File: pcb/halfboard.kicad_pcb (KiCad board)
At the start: 2 copper layers, 117.4 x 87.9 mm, 54 parts, among them U1 

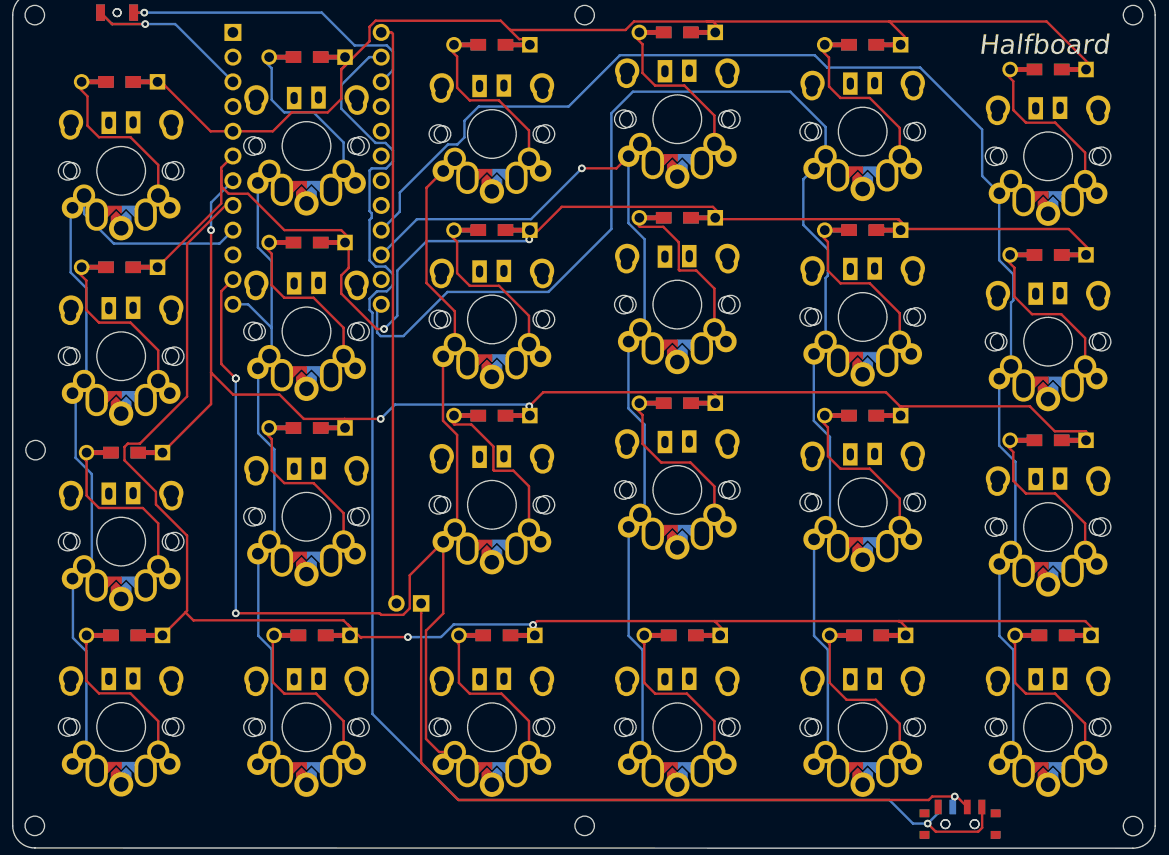
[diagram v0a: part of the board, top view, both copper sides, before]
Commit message: update footprint for better fit
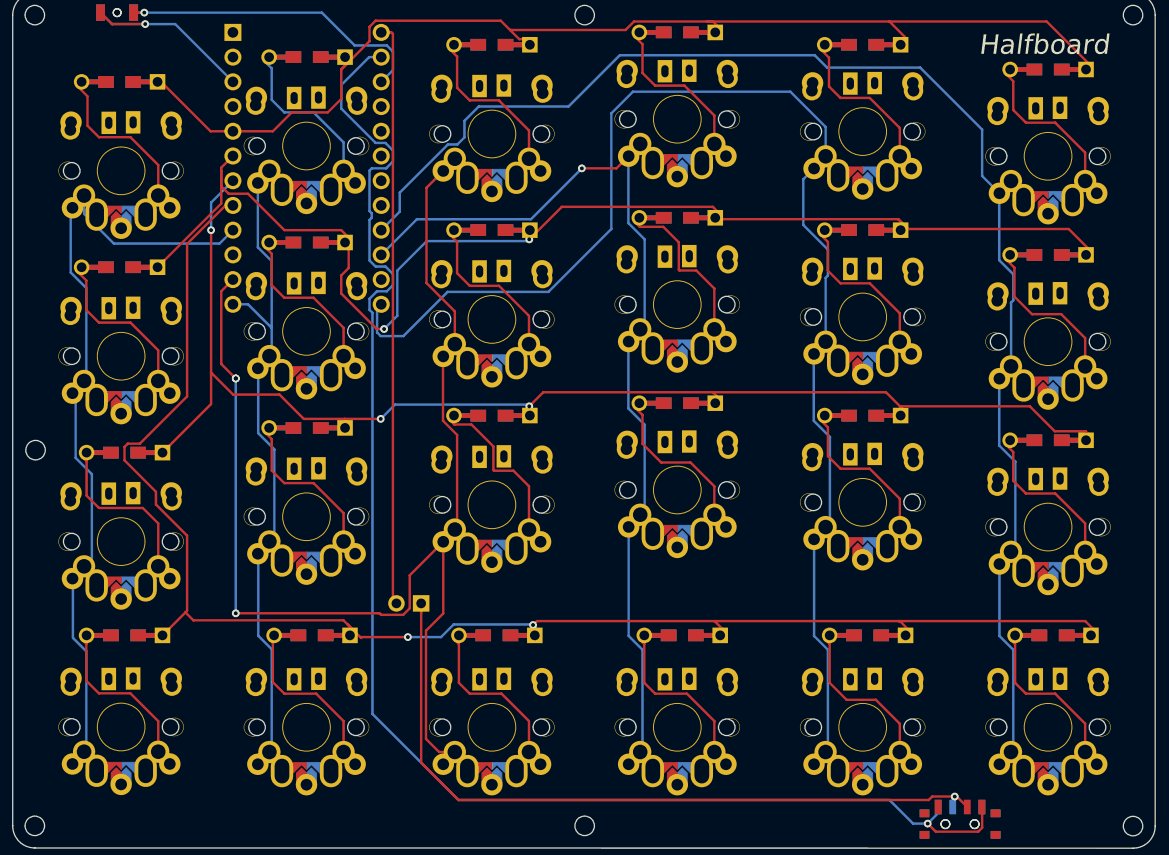
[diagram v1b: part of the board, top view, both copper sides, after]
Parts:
- removed the   at (135.4, 130.6) (x2)
- added  : , Button_Switch_SMD:SW_SPDT_PCM12, F.Cu at (135.4, 130.6)
- added  : , Button_Switch_SMD:SW_SPDT_PCM12, B.Cu at (135.4, 130.6)

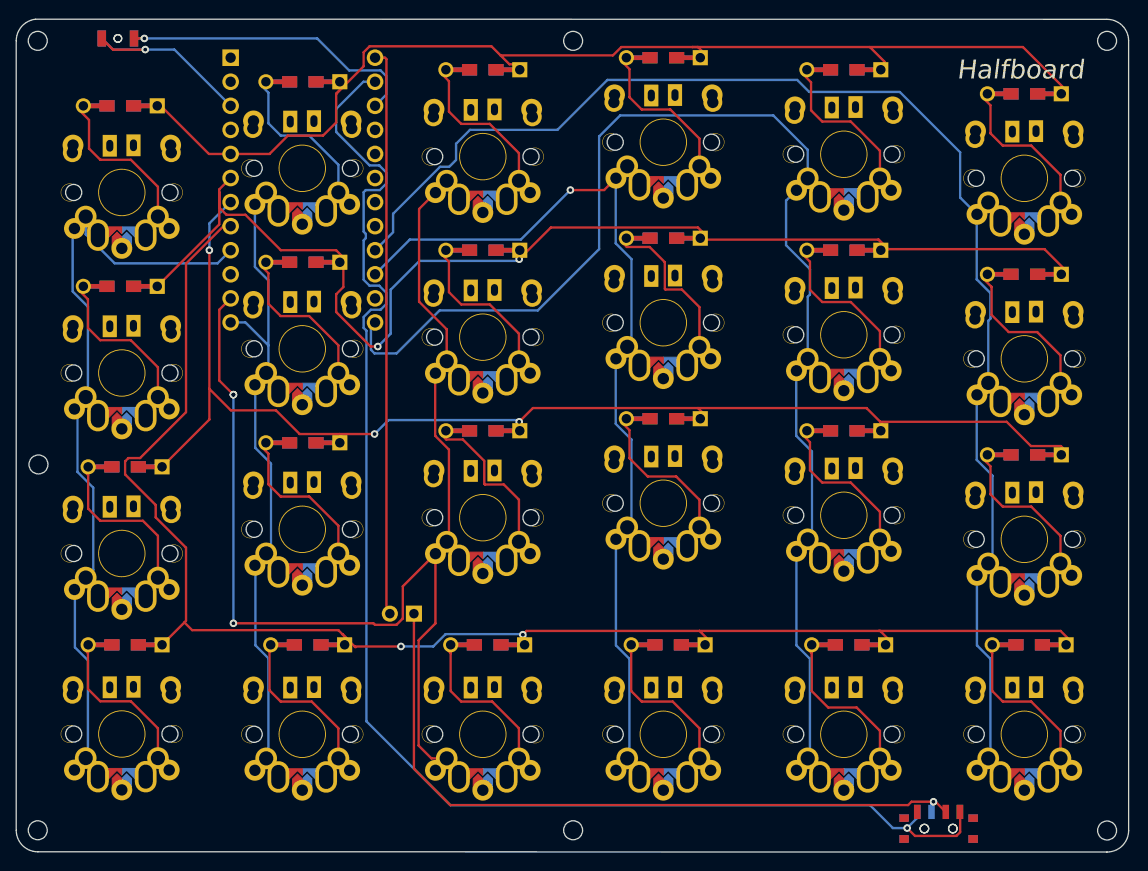
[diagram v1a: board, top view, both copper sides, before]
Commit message: redo routing using freerouting
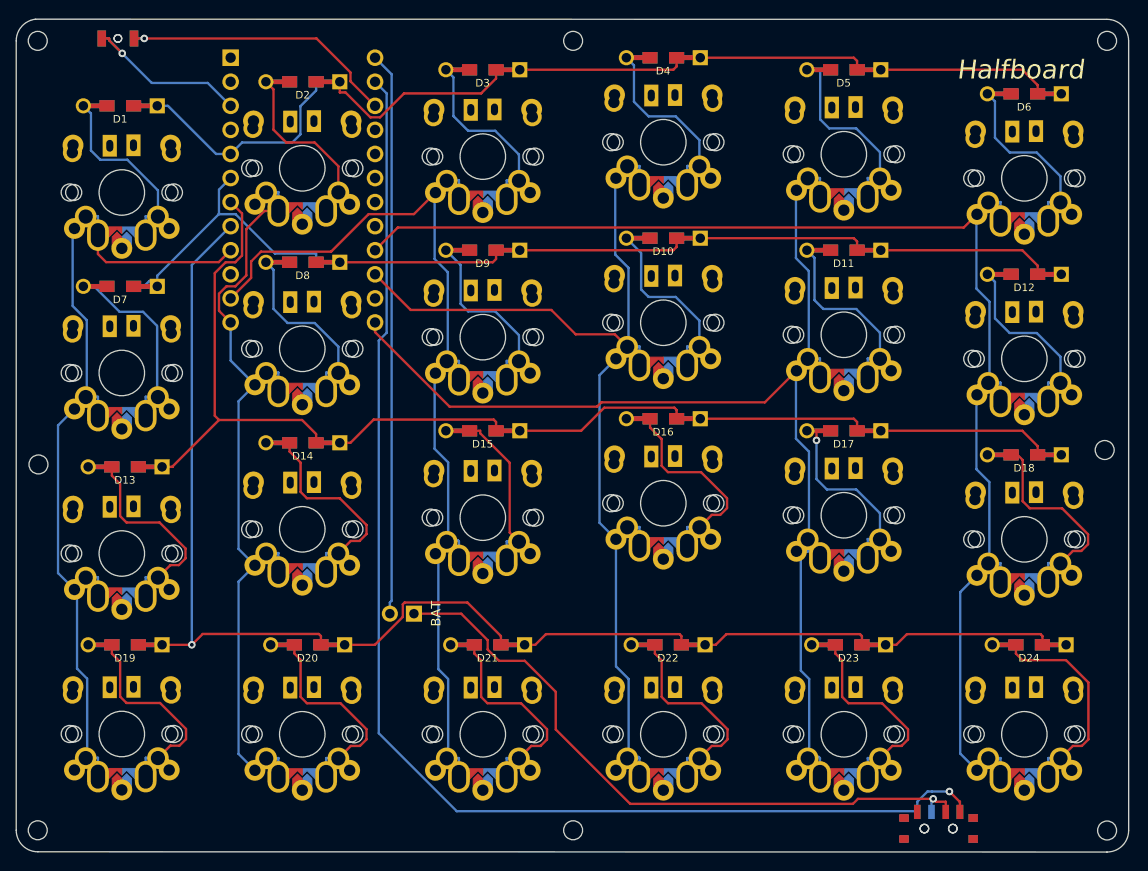
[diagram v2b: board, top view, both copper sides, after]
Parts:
- removed  : , halfboard:MX-ALPs-PG1350-LED-FLIP (x22)
- removed  : , Button_Switch_SMD:SW_SPDT_PCM12 (x2)
- removed  : D, halfboard:Diode-dual (x19)
- removed  : , halfboard:Diode-dual (x3)
- added  D11: , halfboard:Diode-dual, F.Cu at (125.4, 69.8)
- added  D12: , halfboard:Diode-dual, F.Cu at (144.4, 72.4)
- added B.PWR SW: , Button_Switch_SMD:SW_SPDT_PCM12, B.Cu at (135.4, 130.6)
- added D10: , halfboard:Diode-dual, F.Cu at (106.3, 68.6)
- added D13: , halfboard:Diode-dual, F.Cu at (49.5, 92.7)
- added D14: , halfboard:Diode-dual, F.Cu at (68.3, 90.2)
- added D15: , halfboard:Diode-dual, F.Cu at (87.3, 88.9)
- added D16: , halfboard:Diode-dual, F.Cu at (106.3, 87.6)
- added D17: , halfboard:Diode-dual, F.Cu at (125.4, 88.9)
- added D18: , halfboard:Diode-dual, F.Cu at (144.4, 91.4)
- added D19: , halfboard:Diode-dual, F.Cu at (49.5, 111.5)
- added D2: , halfboard:Diode-dual, F.Cu at (68.3, 52.1)
- added D20: , halfboard:Diode-dual, F.Cu at (68.8, 111.5)
- added D21: , halfboard:Diode-dual, F.Cu at (87.8, 111.5)
- added D22: , halfboard:Diode-dual, F.Cu at (106.8, 111.5)
- added D23: , halfboard:Diode-dual, F.Cu at (125.9, 111.5)
- added D24: , halfboard:Diode-dual, F.Cu at (144.9, 111.5)
- added D3: , halfboard:Diode-dual, F.Cu at (87.3, 50.8)
- added D4: , halfboard:Diode-dual, F.Cu at (106.3, 49.5)
- added D5: , halfboard:Diode-dual, F.Cu at (125.4, 50.8)
- added D6: , halfboard:Diode-dual, F.Cu at (144.4, 53.3)
- added D8: , halfboard:Diode-dual, F.Cu at (68.3, 71.1)
- added D9: , halfboard:Diode-dual, F.Cu at (87.3, 69.8)
- added F.PWR SW: , Button_Switch_SMD:SW_SPDT_PCM12, F.Cu at (135.4, 130.6)
- added SW1: , halfboard:MX-ALPs-PG1350-LED-FLIP, F.Cu at (68.2, 61.2)
- added SW10: , halfboard:MX-ALPs-PG1350-LED-FLIP, F.Cu at (125.4, 78.8)
- added SW11: , halfboard:MX-ALPs-PG1350-LED-FLIP, F.Cu at (144.4, 81.3)
- added SW12: , halfboard:MX-ALPs-PG1350-LED-FLIP, F.Cu at (49.2, 101.9)
- added SW13: , halfboard:MX-ALPs-PG1350-LED-FLIP, F.Cu at (68.2, 99.3)
- added SW14: , halfboard:MX-ALPs-PG1350-LED-FLIP, F.Cu at (87.3, 98.1)
- added SW15: , halfboard:MX-ALPs-PG1350-LED-FLIP, F.Cu at (106.3, 96.5)
- added SW16: , halfboard:MX-ALPs-PG1350-LED-FLIP, F.Cu at (125.4, 97.8)
- added SW17: , halfboard:MX-ALPs-PG1350-LED-FLIP, F.Cu at (144.4, 100.4)
- added SW18: , halfboard:MX-ALPs-PG1350-LED-FLIP, F.Cu at (49.2, 120.9)
- added SW19: , halfboard:MX-ALPs-PG1350-LED-FLIP, F.Cu at (68.2, 120.9)
- added SW2: , halfboard:MX-ALPs-PG1350-LED-FLIP, F.Cu at (87.3, 60.0)
- added SW20: , halfboard:MX-ALPs-PG1350-LED-FLIP, F.Cu at (87.3, 120.9)
- added SW21: , halfboard:MX-ALPs-PG1350-LED-FLIP, F.Cu at (106.3, 120.9)
- added SW22: , halfboard:MX-ALPs-PG1350-LED-FLIP, F.Cu at (125.4, 120.9)
- added SW23: , halfboard:MX-ALPs-PG1350-LED-FLIP, F.Cu at (144.4, 120.9)
- added SW3: , halfboard:MX-ALPs-PG1350-LED-FLIP, F.Cu at (106.3, 58.4)
- added SW4: , halfboard:MX-ALPs-PG1350-LED-FLIP, F.Cu at (125.4, 59.7)
- added SW5: , halfboard:MX-ALPs-PG1350-LED-FLIP, F.Cu at (144.4, 62.3)
- added SW7: , halfboard:MX-ALPs-PG1350-LED-FLIP, F.Cu at (68.2, 80.3)
- added SW8: , halfboard:MX-ALPs-PG1350-LED-FLIP, F.Cu at (87.3, 79.0)
- added SW9: , halfboard:MX-ALPs-PG1350-LED-FLIP, F.Cu at (106.3, 77.5)
- B.RST, BAT, D1, D7, F.RST, SW0, SW6: renamed from  
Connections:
- D1 pad 1: (no net) -> row0
- D1 pad 2: (no net) -> col0_row0
- D7 pad 1: (no net) -> row1
- D7 pad 2: (no net) -> col0_row1
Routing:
- net col3: track 90.8 -> 112.5 mm, vias 1 -> 0
- net col1: track 66.7 -> 87.7 mm
- net col2: track 126.4 -> 106.9 mm, vias 3 -> 0
- net col0: track 80.0 -> 94.6 mm
- net BAT_GND: track 150.2 -> 137.4 mm
- net row0: track 117.9 -> 129.0 mm
- net col5_row3: track 16.9 -> 27.2 mm
- net col4_row1: track 16.6 -> 26.7 mm
- net col0_row1: track 17.0 -> 27.1 mm
- net col5_row2: track 16.6 -> 26.5 mm
- net col1_row1: track 16.8 -> 26.6 mm
- net col5_row0: track 16.6 -> 26.4 mm
- net col2_row0: track 16.8 -> 26.6 mm
- net col2_row1: track 16.8 -> 26.6 mm
- net col3_row0: track 16.6 -> 26.4 mm
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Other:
- outline, holes or cut-outs redrawn

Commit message: create schematics and assign footprints in pcb
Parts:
- removed the D1 at (49.0, 54.6)
- removed the D10 at (106.3, 68.6)
- removed the D13 at (49.5, 92.7)
- removed the D14 at (68.3, 90.2)
- removed the D15 at (87.3, 88.9)
- removed the D16 at (106.3, 87.6)
- removed the D17 at (125.4, 88.9)
- removed the D18 at (144.4, 91.4)
- removed the D19 at (49.5, 111.5)
- removed the D2 at (68.3, 52.1)
- removed the D20 at (68.8, 111.5)
- removed the D21 at (87.8, 111.5)
- removed the D22 at (106.8, 111.5)
- removed the D23 at (125.9, 111.5)
- removed the D24 at (144.9, 111.5)
- removed the D3 at (87.3, 50.8)
- removed the D4 at (106.3, 49.5)
- removed the D5 at (125.4, 50.8)
- removed the D6 at (144.4, 53.3)
- removed the D7 at (49.0, 73.7)
- removed the D8 at (68.3, 71.1)
- removed the D9 at (87.3, 69.8)
- removed SW0: , halfboard:MX-ALPs-PG1350-LED-FLIP
- removed the SW1 at (68.2, 61.2)
- removed the SW10 at (125.4, 78.8)
- removed the SW11 at (144.4, 81.3)
- removed the SW12 at (49.2, 101.9)
- removed the SW13 at (68.2, 99.3)
- removed the SW14 at (87.3, 98.1)
- removed the SW15 at (106.3, 96.5)
- removed the SW16 at (125.4, 97.8)
- removed the SW17 at (144.4, 100.4)
- removed the SW18 at (49.2, 120.9)
- removed the SW19 at (68.2, 120.9)
- removed the SW2 at (87.3, 60.0)
- removed the SW20 at (87.3, 120.9)
- removed the SW21 at (106.3, 120.9)
- removed the SW22 at (125.4, 120.9)
- removed the SW23 at (144.4, 120.9)
- removed the SW3 at (106.3, 58.4)
- removed the SW4 at (125.4, 59.7)
- removed the SW5 at (144.4, 62.3)
- removed the SW6 at (49.2, 82.8)
- removed the SW7 at (68.2, 80.3)
- removed the SW8 at (87.3, 79.0)
- removed the SW9 at (106.3, 77.5)
- removed the U1 at (68.3, 63.5)
- added  : , halfboard:MX-ALPs-PG1350-LED-FLIP-PLATE, F.Cu at (205.6, 106.4)
- added  : , halfboard:MX-ALPs-PG1350-LED-FLIP-PLATE, F.Cu at (262.8, 120.1)
- added  : , halfboard:MX-ALPs-PG1350-LED-FLIP-PLATE, F.Cu at (224.7, 122.9)
- added  : , halfboard:MX-ALPs-PG1350-LED-FLIP-PLATE, F.Cu at (281.8, 102.4)
- added  : , halfboard:MX-ALPs-PG1350-LED-FLIP-PLATE, F.Cu at (300.9, 124.0)
- added  : , halfboard:MX-ALPs-PG1350-LED-FLIP-PLATE, F.Cu at (300.9, 144.5)
- added  : , halfboard:MX-ALPs-PG1350-LED-FLIP-PLATE, F.Cu at (224.7, 144.5)
- added  : , halfboard:MX-ALPs-PG1350-LED-FLIP-PLATE, F.Cu at (262.8, 82.0)
- added  : , halfboard:MX-ALPs-PG1350-LED-FLIP-PLATE, F.Cu at (243.7, 83.6)
- added  : , halfboard:MX-ALPs-PG1350-LED-FLIP-PLATE, F.Cu at (281.8, 121.4)
- added  : , halfboard:MX-ALPs-PG1350-LED-FLIP-PLATE, F.Cu at (205.6, 125.5)
- added  : , halfboard:MX-ALPs-PG1350-LED-FLIP-PLATE, F.Cu at (262.8, 101.1)
- added  : , halfboard:MX-ALPs-PG1350-LED-FLIP-PLATE, F.Cu at (205.6, 144.5)
- added  : , halfboard:MX-ALPs-PG1350-LED-FLIP-PLATE, F.Cu at (224.7, 103.8)
- added  : , halfboard:MX-ALPs-PG1350-LED-FLIP-PLATE, F.Cu at (224.7, 84.8)
- added  : , halfboard:MX-ALPs-PG1350-LED-FLIP-PLATE, F.Cu at (281.8, 144.5)
- added  : , halfboard:MX-ALPs-PG1350-LED-FLIP-PLATE, F.Cu at (300.9, 104.9)
- added  : , halfboard:MX-ALPs-PG1350-LED-FLIP-PLATE, F.Cu at (243.7, 102.6)
- added  : , halfboard:MX-ALPs-PG1350-LED-FLIP-PLATE, F.Cu at (262.8, 144.5)
- added  : , halfboard:MX-ALPs-PG1350-LED-FLIP-PLATE, F.Cu at (300.9, 85.9)
- added  : , halfboard:MX-ALPs-PG1350-LED-FLIP-PLATE, F.Cu at (243.7, 121.7)
- added  : , halfboard:MX-ALPs-PG1350-LED-FLIP-PLATE, F.Cu at (205.6, 87.4)
- added  : , halfboard:MX-ALPs-PG1350-LED-FLIP-PLATE, F.Cu at (281.8, 83.3)
- added  : , halfboard:MX-ALPs-PG1350-LED-FLIP-PLATE, F.Cu at (243.7, 144.5)
- added BAT1: Battery, Connector_PinHeader_2.54mm:PinHeader_1x02_P2.54mm_Vertical, F.Cu at (234.9, 131.7)
- added D1: 1N4148W, halfboard:Diode-dual, F.Cu at (184.3, 96.9)
- added D1: , halfboard:Diode-dual, F.Cu at (27.5, 116.9)
- added D10: 1N4148W, halfboard:Diode-dual, F.Cu at (176.1, 94.3)
- added D10: , halfboard:Diode-dual, F.Cu at (84.8, 130.9)
- added D11: 1N4148W, halfboard:Diode-dual, F.Cu at (173.3, 77.3)
- added D12: 1N4148W, halfboard:Diode-dual, F.Cu at (121.9, 97.8)
- added D13: 1N4148W, halfboard:Diode-dual, F.Cu at (163.5, 102.1)
- added D13: , halfboard:Diode-dual, F.Cu at (28.0, 155.0)
- added D14: 1N4148W, halfboard:Diode-dual, F.Cu at (132.3, 97.8)
- added D14: , halfboard:Diode-dual, F.Cu at (46.8, 152.5)
- added D15: 1N4148W, halfboard:Diode-dual, F.Cu at (132.3, 100.4)
- added D15: , halfboard:Diode-dual, F.Cu at (65.8, 151.2)
- added D16: 1N4148W, halfboard:Diode-dual, F.Cu at (155.3, 94.3)
- added D16: , halfboard:Diode-dual, F.Cu at (84.8, 149.9)
- added D17: 1N4148W, halfboard:Diode-dual, F.Cu at (142.7, 97.8)
- added D17: , halfboard:Diode-dual, F.Cu at (103.9, 151.2)
- added D18: 1N4148W, halfboard:Diode-dual, F.Cu at (153.1, 97.8)
- added D18: , halfboard:Diode-dual, F.Cu at (122.9, 153.7)
- added D19: 1N4148W, halfboard:Diode-dual, F.Cu at (142.7, 100.4)
- added D19: , halfboard:Diode-dual, F.Cu at (28.0, 173.8)
- added D2: 1N4148W, halfboard:Diode-dual, F.Cu at (173.3, 87.7)
- added D2: , halfboard:Diode-dual, F.Cu at (46.8, 114.4)
- added D20: 1N4148W, halfboard:Diode-dual, F.Cu at (165.7, 94.3)
- added D20: , halfboard:Diode-dual, F.Cu at (47.3, 173.8)
- added D21: 1N4148W, halfboard:Diode-dual, F.Cu at (153.1, 100.4)
- added D21: , halfboard:Diode-dual, F.Cu at (66.3, 173.8)
- added D22: 1N4148W, halfboard:Diode-dual, F.Cu at (163.5, 96.9)
- added D22: , halfboard:Diode-dual, F.Cu at (85.3, 173.8)
- added D23: 1N4148W, halfboard:Diode-dual, F.Cu at (163.5, 99.5)
- added D23: , halfboard:Diode-dual, F.Cu at (104.4, 173.8)
- added D24: 1N4148W, halfboard:Diode-dual, F.Cu at (121.9, 100.4)
- added D24: , halfboard:Diode-dual, F.Cu at (123.4, 173.8)
- added D3: 1N4148W, halfboard:Diode-dual, F.Cu at (173.3, 85.1)
- added D3: , halfboard:Diode-dual, F.Cu at (65.8, 113.1)
- added D4: 1N4148W, halfboard:Diode-dual, F.Cu at (173.3, 82.5)
- added D4: , halfboard:Diode-dual, F.Cu at (84.8, 111.8)
- added D5: 1N4148W, halfboard:Diode-dual, F.Cu at (173.3, 79.9)
- added D5: , halfboard:Diode-dual, F.Cu at (103.9, 113.1)
- added D6: 1N4148W, halfboard:Diode-dual, F.Cu at (173.9, 102.1)
- added D6: , halfboard:Diode-dual, F.Cu at (122.9, 115.6)
- added D7: 1N4148W, halfboard:Diode-dual, F.Cu at (173.9, 99.5)
- added D7: , halfboard:Diode-dual, F.Cu at (27.5, 136.0)
- added D8: 1N4148W, halfboard:Diode-dual, F.Cu at (173.9, 96.9)
- added D8: , halfboard:Diode-dual, F.Cu at (46.8, 133.4)
- added D9: 1N4148W, halfboard:Diode-dual, F.Cu at (186.5, 94.3)
- added D9: , halfboard:Diode-dual, F.Cu at (65.8, 132.2)
- added PWR_SW1: SW_SPST, Button_Switch_SMD:SW_SPDT_PCM12, F.Cu at (291.6, 154.2)
- added PWR_SW2: SW_SPST, Button_Switch_SMD:SW_SPDT_PCM12, B.Cu at (291.6, 154.3)
- added RESET1: SW_PUSH, Button_Switch_SMD:SW_SPST_TL3342, F.Cu at (205.9, 74.6)
- added RESET2: SW_PUSH, Button_Switch_SMD:SW_SPST_TL3342, B.Cu at (205.9, 74.6)
- added SW1: SW_PUSH, halfboard:MX-ALPs-PG1350-LED-FLIP, F.Cu at (205.6, 87.4)
- added SW1: , halfboard:MX-ALPs-PG1350-LED-FLIP, F.Cu at (27.7, 126.1)
- added SW10: SW_PUSH, halfboard:MX-ALPs-PG1350-LED-FLIP, F.Cu at (263.1, 99.0)
- added SW10: , halfboard:MX-ALPs-PG1350-LED-FLIP, F.Cu at (84.8, 139.8)
- added SW11: SW_PUSH, halfboard:MX-ALPs-PG1350-LED-FLIP, F.Cu at (283.0, 99.7)
- added SW11: , halfboard:MX-ALPs-PG1350-LED-FLIP, F.Cu at (103.9, 141.1)
- added SW12: SW_PUSH, halfboard:MX-ALPs-PG1350-LED-FLIP, F.Cu at (302.4, 101.4)
- added SW12: , halfboard:MX-ALPs-PG1350-LED-FLIP, F.Cu at (122.9, 143.6)
- added SW13: SW_PUSH, halfboard:MX-ALPs-PG1350-LED-FLIP, F.Cu at (205.6, 125.5)
- added SW13: , halfboard:MX-ALPs-PG1350-LED-FLIP, F.Cu at (27.7, 164.2)
- added SW14: SW_PUSH, halfboard:MX-ALPs-PG1350-LED-FLIP, F.Cu at (224.6, 122.9)
- added SW14: , halfboard:MX-ALPs-PG1350-LED-FLIP, F.Cu at (46.7, 161.6)
- added SW15: SW_PUSH, halfboard:MX-ALPs-PG1350-LED-FLIP, F.Cu at (245.0, 117.7)
- added SW15: , halfboard:MX-ALPs-PG1350-LED-FLIP, F.Cu at (65.8, 160.4)
- added SW16: SW_PUSH, halfboard:MX-ALPs-PG1350-LED-FLIP, F.Cu at (263.2, 116.7)
- added SW16: , halfboard:MX-ALPs-PG1350-LED-FLIP, F.Cu at (84.8, 158.9)
- added SW17: SW_PUSH, halfboard:MX-ALPs-PG1350-LED-FLIP, F.Cu at (283.3, 117.7)
- added SW17: , halfboard:MX-ALPs-PG1350-LED-FLIP, F.Cu at (103.9, 160.1)
- added SW18: SW_PUSH, halfboard:MX-ALPs-PG1350-LED-FLIP, F.Cu at (302.8, 120.7)
- added SW18: , halfboard:MX-ALPs-PG1350-LED-FLIP, F.Cu at (122.9, 162.7)
- added SW19: SW_PUSH, halfboard:MX-ALPs-PG1350-LED-FLIP, F.Cu at (205.6, 144.5)
- added SW19: , halfboard:MX-ALPs-PG1350-LED-FLIP, F.Cu at (27.7, 183.2)
- added SW2: SW_PUSH, halfboard:MX-ALPs-PG1350-LED-FLIP, F.Cu at (224.8, 84.9)
- added SW2: , halfboard:MX-ALPs-PG1350-LED-FLIP, F.Cu at (46.7, 123.5)
- added SW20: SW_PUSH, halfboard:MX-ALPs-PG1350-LED-FLIP, F.Cu at (224.7, 144.5)
- added SW20: , halfboard:MX-ALPs-PG1350-LED-FLIP, F.Cu at (46.7, 183.2)
- added SW21: SW_PUSH, halfboard:MX-ALPs-PG1350-LED-FLIP, F.Cu at (244.3, 145.0)
- added SW21: , halfboard:MX-ALPs-PG1350-LED-FLIP, F.Cu at (65.8, 183.2)
- added SW22: SW_PUSH, halfboard:MX-ALPs-PG1350-LED-FLIP, F.Cu at (262.4, 133.3)
- added SW22: , halfboard:MX-ALPs-PG1350-LED-FLIP, F.Cu at (84.8, 183.2)
- added SW23: SW_PUSH, halfboard:MX-ALPs-PG1350-LED-FLIP, F.Cu at (283.0, 135.0)
- added SW23: , halfboard:MX-ALPs-PG1350-LED-FLIP, F.Cu at (103.9, 183.2)
- added SW24: SW_PUSH, halfboard:MX-ALPs-PG1350-LED-FLIP, F.Cu at (303.0, 137.0)
- added SW24: , halfboard:MX-ALPs-PG1350-LED-FLIP, F.Cu at (122.9, 183.2)
- added SW3: SW_PUSH, halfboard:MX-ALPs-PG1350-LED-FLIP, F.Cu at (244.0, 83.7)
- added SW3: , halfboard:MX-ALPs-PG1350-LED-FLIP, F.Cu at (65.8, 122.3)
- added SW4: SW_PUSH, halfboard:MX-ALPs-PG1350-LED-FLIP, F.Cu at (261.6, 82.5)
- added SW4: , halfboard:MX-ALPs-PG1350-LED-FLIP, F.Cu at (84.8, 120.8)
- added SW5: SW_PUSH, halfboard:MX-ALPs-PG1350-LED-FLIP, F.Cu at (281.8, 84.0)
- added SW5: , halfboard:MX-ALPs-PG1350-LED-FLIP, F.Cu at (103.9, 122.0)
- added SW6: SW_PUSH, halfboard:MX-ALPs-PG1350-LED-FLIP, F.Cu at (300.5, 85.6)
- added SW6: , halfboard:MX-ALPs-PG1350-LED-FLIP, F.Cu at (122.9, 124.6)
- added SW7: SW_PUSH, halfboard:MX-ALPs-PG1350-LED-FLIP, F.Cu at (205.5, 106.5)
- added SW7: , halfboard:MX-ALPs-PG1350-LED-FLIP, F.Cu at (27.7, 145.1)
- added SW8: SW_PUSH, halfboard:MX-ALPs-PG1350-LED-FLIP, F.Cu at (224.7, 103.9)
- added SW8: , halfboard:MX-ALPs-PG1350-LED-FLIP, F.Cu at (46.7, 142.6)
- added SW9: SW_PUSH, halfboard:MX-ALPs-PG1350-LED-FLIP, F.Cu at (244.5, 100.7)
- added SW9: , halfboard:MX-ALPs-PG1350-LED-FLIP, F.Cu at (65.8, 141.3)
- added U1: ProMicro, halfboard:ArduinoProMicro-TopSide, F.Cu at (224.5, 87.8)
- added U1: , halfboard:ArduinoProMicro-TopSide, F.Cu at (46.8, 125.8)
- moved  D11 65.9 mm to (103.9, 132.2)
- moved  D12 65.9 mm to (122.9, 134.7)
- moved BAT 65.9 mm to (58.5, 170.5)
- moved B.PWR SW 65.9 mm to (113.9, 192.9)
- moved B.RST 65.9 mm to (27.3, 109.8)
- moved F.PWR SW 65.9 mm to (113.9, 192.9)
- moved F.RST 65.9 mm to (27.3, 109.8)
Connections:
-  D11 pad 1: row1 -> (no net)
-  D11 pad 2: col4_row1 -> (no net)
-  D12 pad 1: row1 -> (no net)
-  D12 pad 2: col5_row1 -> (no net)
- B.PWR SW pad 2: BAT_SW -> (no net)
- B.PWR SW pad 3: BAT_GND -> (no net)
- B.RST pad 1: RESET -> (no net)
- B.RST pad 2: RESET_GND -> (no net)
- BAT pad 1: BAT_SW -> (no net)
- BAT pad 2: BAT0 -> (no net)
- F.PWR SW pad 2: BAT_SW -> (no net)
- F.PWR SW pad 3: BAT_GND -> (no net)
- F.RST pad 1: RESET_GND -> (no net)
- F.RST pad 2: RESET -> (no net)
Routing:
- net (no net): track 0.00 -> 2162.9 mm, vias 0 -> 6
- net row3: track 154.7 -> 0.00 mm, vias 1 -> 0
- net col5: track 144.0 -> 0.00 mm
- net BAT_GND: track 137.4 -> 0.00 mm, vias 1 -> 0
- net row2: track 133.2 -> 0.00 mm
- net row0: track 129.0 -> 0.00 mm
- net row1: track 128.7 -> 0.00 mm
- net col4: track 128.7 -> 0.00 mm
- net col3: track 112.5 -> 0.00 mm
- net col2: track 106.9 -> 0.00 mm
- net col0: track 94.6 -> 0.00 mm
- net col1: track 87.7 -> 0.00 mm
- net BAT_SW: track 70.2 -> 0.00 mm, vias 1 -> 0
- net BAT0: track 59.5 -> 0.00 mm
- net RESET: track 30.0 -> 0.00 mm, vias 1 -> 0
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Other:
- board size 117.4 x 87.9 mm -> 295.4 x 126.6 mm

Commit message: finish pcb using new schematics
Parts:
- removed  D11: , halfboard:Diode-dual
- removed  D12: , halfboard:Diode-dual
- removed B.PWR SW: , Button_Switch_SMD:SW_SPDT_PCM12
- removed B.RST, F.RST: , Button_Switch_SMD:SW_SPST_B3U-3000P-B
- removed BAT: , Connector_PinHeader_2.54mm:PinHeader_1x02_P2.54mm_Vertical
- removed the D1 at (27.5, 116.9)
- removed the D10 at (84.8, 130.9)
- removed the D13 at (28.0, 155.0)
- removed the D14 at (46.8, 152.5)
- removed the D15 at (65.8, 151.2)
- removed the D16 at (84.8, 149.9)
- removed the D17 at (103.9, 151.2)
- removed the D18 at (122.9, 153.7)
- removed the D19 at (28.0, 173.8)
- removed the D2 at (46.8, 114.4)
- removed the D20 at (47.3, 173.8)
- removed the D21 at (66.3, 173.8)
- removed the D22 at (85.3, 173.8)
- removed the D23 at (104.4, 173.8)
- removed the D24 at (123.4, 173.8)
- removed the D3 at (65.8, 113.1)
- removed the D4 at (84.8, 111.8)
- removed the D5 at (103.9, 113.1)
- removed the D6 at (122.9, 115.6)
- removed the D7 at (27.5, 136.0)
- removed the D8 at (46.8, 133.4)
- removed the D9 at (65.8, 132.2)
- removed F.PWR SW: , Button_Switch_SMD:SW_SPDT_PCM12
- removed the SW1 at (27.7, 126.1)
- removed the SW10 at (84.8, 139.8)
- removed the SW11 at (103.9, 141.1)
- removed the SW12 at (122.9, 143.6)
- removed the SW13 at (27.7, 164.2)
- removed the SW14 at (46.7, 161.6)
- removed the SW15 at (65.8, 160.4)
- removed the SW16 at (84.8, 158.9)
- removed the SW17 at (103.9, 160.1)
- removed the SW18 at (122.9, 162.7)
- removed the SW19 at (27.7, 183.2)
- removed the SW2 at (46.7, 123.5)
- removed the SW20 at (46.7, 183.2)
- removed the SW21 at (65.8, 183.2)
- removed the SW22 at (84.8, 183.2)
- removed the SW23 at (103.9, 183.2)
- removed the SW24 at (122.9, 183.2)
- removed the SW3 at (65.8, 122.3)
- removed the SW4 at (84.8, 120.8)
- removed the SW5 at (103.9, 122.0)
- removed the SW6 at (122.9, 124.6)
- removed the SW7 at (27.7, 145.1)
- removed the SW8 at (46.7, 142.6)
- removed the SW9 at (65.8, 141.3)
- removed the U1 at (46.8, 125.8)
- moved SW18 109.4 mm to (194.5, 105.4), turned to 180 degrees
- moved SW24 109.0 mm to (194.5, 126.0), turned to 180 degrees
- moved SW12 109.0 mm to (194.5, 86.4), turned to 180 degrees
- moved SW17 108.9 mm to (175.4, 102.9), turned to 180 degrees
- moved SW11 108.8 mm to (175.4, 83.8), turned to 180 degrees
- moved SW21 108.7 mm to (137.3, 126.0), turned to 180 degrees
- moved SW15 108.7 mm to (137.3, 103.1), turned to 180 degrees
- moved SW9 108.4 mm to (137.3, 84.1), turned to 180 degrees
- moved SW3 108.3 mm to (137.3, 65.0), turned to 180 degrees
- moved SW2 108.1 mm to (118.3, 66.3), turned to 180 degrees
- moved SW5 108.1 mm to (175.4, 64.8), turned to 180 degrees
- moved SW8 108.0 mm to (118.3, 85.3), turned to 180 degrees
- moved   108.0 mm to (156.4, 101.6)
- moved   108.0 mm to (175.4, 83.8)
- moved   108.0 mm to (156.4, 63.5)
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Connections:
- net VCC renamed Net-(U1-Pad21)
- U1 pad 11: col1 -> Net-(U1-Pad11)
- U1 pad 12: col2 -> Net-(U1-Pad12)
- U1 pad 15: Net-(U1-Pad15) -> col5
- U1 pad 16: Net-(U1-Pad16) -> col4
- U1 pad 17: Net-(U1-Pad17) -> col3
- U1 pad 18: col5 -> col2
- U1 pad 19: col4 -> col1
- U1 pad 20: col3 -> col0
- U1 pad 9: col0 -> Net-(U1-Pad9)
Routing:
- net (no net): track 2162.9 -> 0.00 mm, vias 6 -> 0
- net GND: track 0.00 -> 218.1 mm, vias 0 -> 2
- net row3: track 0.00 -> 149.6 mm
- net row2: track 0.00 -> 146.0 mm
- net row1: track 0.00 -> 130.0 mm
- net col5: track 0.00 -> 129.1 mm
- net col4: track 0.00 -> 119.7 mm, vias 0 -> 2
- net row0: track 0.00 -> 118.9 mm
- net col3: track 0.00 -> 94.0 mm
- net col0: track 0.00 -> 90.9 mm
- net Net-(BAT1-Pad2): track 0.00 -> 78.0 mm, vias 0 -> 1
- net col1: track 0.00 -> 73.6 mm
- net col2: track 0.00 -> 65.4 mm
- net bat: track 0.00 -> 59.6 mm
- net reset: track 0.00 -> 34.0 mm, vias 0 -> 1
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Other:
- board size 295.4 x 126.6 mm -> 117.4 x 87.9 mm
